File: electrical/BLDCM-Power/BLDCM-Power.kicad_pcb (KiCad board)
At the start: 4 copper layers, 32 x 32 mm, 37 parts, among them J1 501920-3001, J2 53048-0310, J3 53261-0471, J4 53261-0471, J5 FTSH-107-01-L-DV-K, J6 12402012E212A, U1 INA239-Q1, U2 LDL212PV33R, U3 TMC6300-LA, U4 INA239-Q1, U5 TCAN1462, U6 INA239-Q1

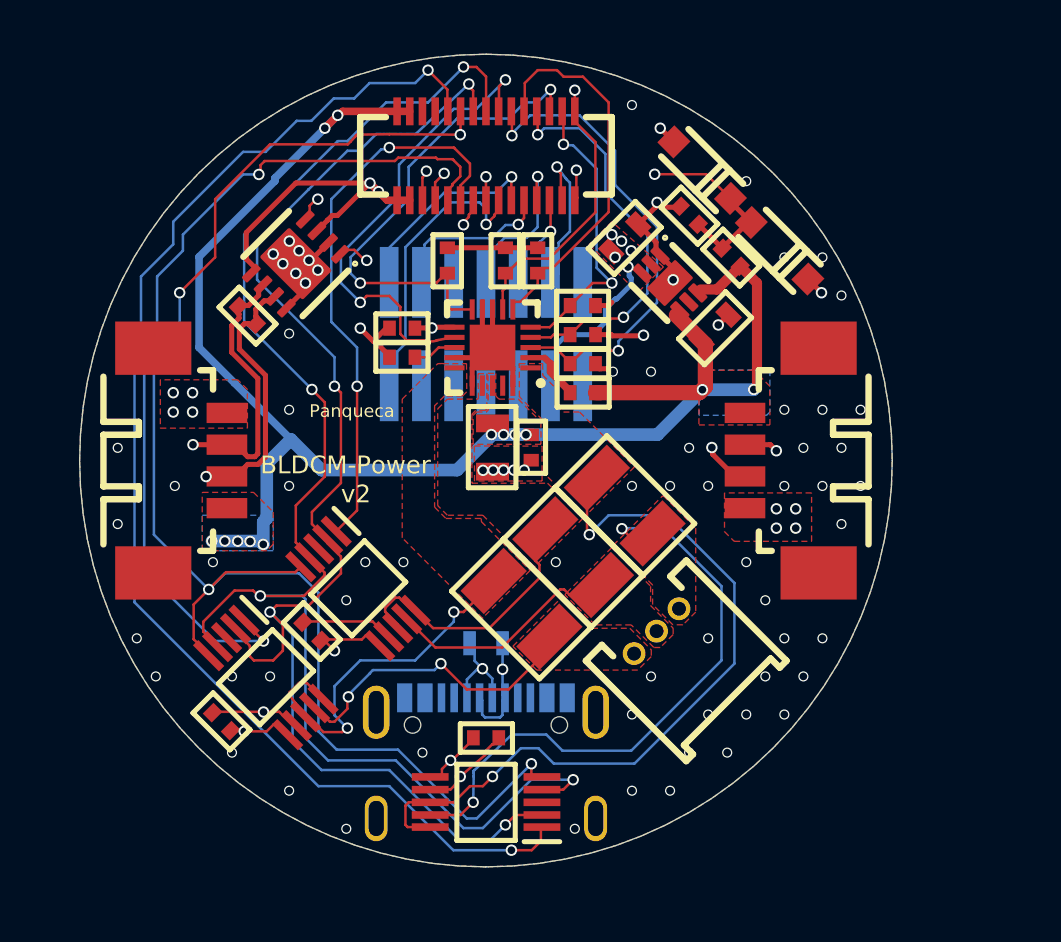
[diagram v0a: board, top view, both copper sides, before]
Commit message: Fix: PCB resistor rotation
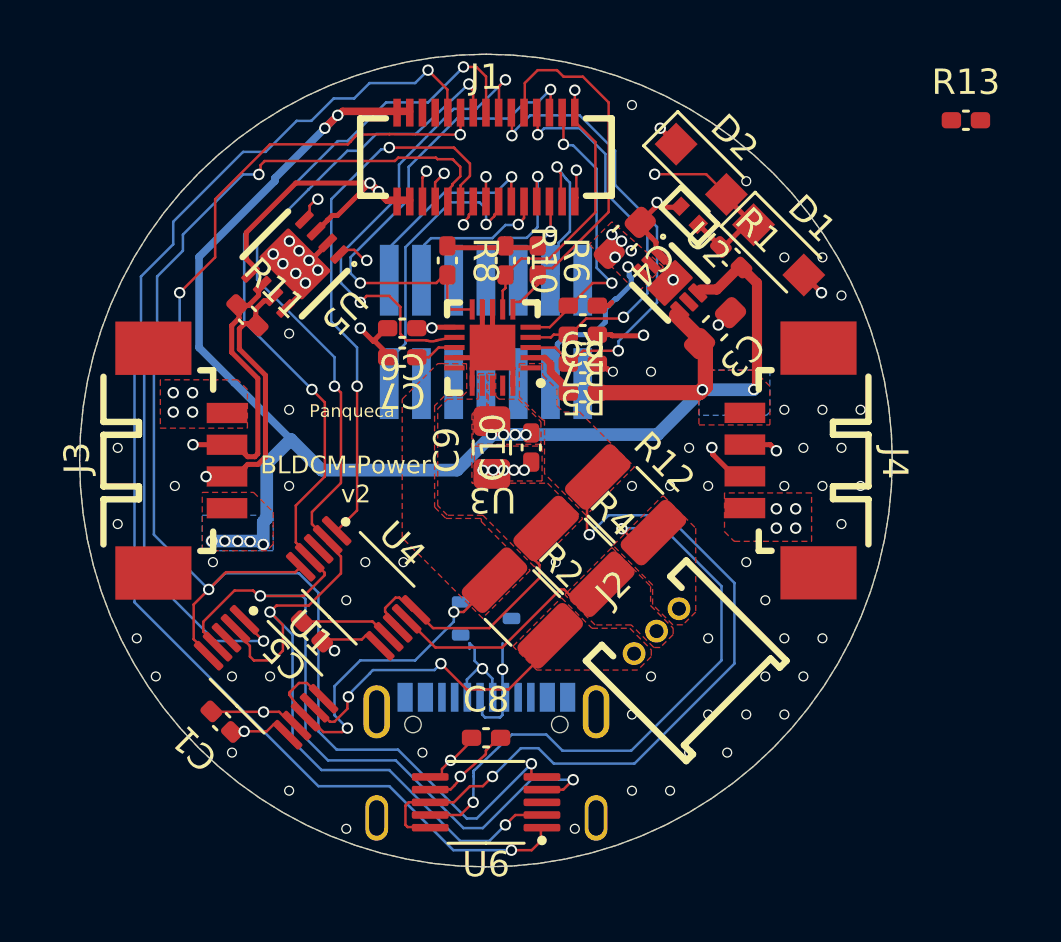
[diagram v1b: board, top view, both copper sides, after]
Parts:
- added R13: 10K, BrenoCQ:R_0402, F.Cu at (167.4, 91.6)
- C1, C10, C2, C5, C6, C7, C8: footprint brenocqLib:CAP_0402 -> BrenoCQ:C_0402
- C3, C4: footprint brenocqLib:CAP_0603 -> BrenoCQ:C_0603
- C9: footprint brenocqLib:CAP_0805 -> BrenoCQ:C_0805
- D1, D2: footprint brenocqLib:SOD-123 -> BrenoCQ:SOD-123
- D3: footprint brenocqLib:SOT-323-3 -> BrenoCQ:SOT-323
- J1: footprint brenocqLib:501920-3001 -> BrenoCQ:501920-3001
- J2: footprint brenocqLib:53048-0310 -> BrenoCQ:53048-0310
- J3, J4: footprint brenocqLib:MOLEX_125MM_4P_H_SMD -> BrenoCQ:53261-0471
- J5: footprint brenocqLib:FTSH-107-01-L-DV-K-TR -> BrenoCQ:FTSH-107-01-L-DV-K-TR
- J6: footprint brenocqLib:12402012E212A -> BrenoCQ:12402012E212A
- R1, R10, R11, R5, R6, R7, R8, R9: footprint brenocqLib:RES_0402 -> BrenoCQ:R_0402
- R12, R2, R4: footprint brenocqLib:RES_1210 -> BrenoCQ:R_1210
- U1, U4, U6: footprint brenocqLib:VSSOP-10 -> BrenoCQ:VSSOP-10
- U2: footprint brenocqLib:DFN-6-2x2 -> BrenoCQ:DFN-6-2x2
- U3: footprint brenocqLib:QFN-20 -> BrenoCQ:QFN-20
- U5: footprint brenocqLib:VSON-8 -> BrenoCQ:VSON-8
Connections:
- net CAN.RX renamed /CAN.RX
- net CAN.TX renamed /CAN.TX
- net INA.CLK renamed /INA.CLK
- net INA.CS0 renamed /INA.CS0
- net INA.CS1 renamed /INA.CS1
- net INA.CS2 renamed /INA.CS2
- net INA.PICO renamed /INA.PICO
- net INA.POCI renamed /INA.POCI
- net NetC7_1 renamed Net-(U3-1.8VOUT)
- net RST renamed /RST
- net SWCLK renamed /SWCLK
- net SWDIO renamed /SWDIO
- net SWO renamed /SWO
- net TCM.DIAG renamed /TCM.DIAG
- net TCM.U.IN renamed /TCM.U.IN
- net TCM.U.OUT renamed /TCM.U.OUT
- net TCM.V.IN renamed /TCM.V.IN
- net TCM.V.OUT renamed /TCM.V.OUT
- net TCM.W.IN renamed /TCM.W.IN
- net TCM.W.OUT renamed /TCM.W.OUT
- net USB_N renamed /USB_N
- net USB_P renamed /USB_P
- net VCP.RX renamed /VCP.RX
- net VCP.TX renamed /VCP.TX
- C1 pad 1: 3.3V -> GND
- C1 pad 2: GND -> 3.3V
- C10 pad 1: GND -> VIN
- C10 pad 2: VIN -> GND
- C2 pad 1: NetC2_1 -> VIN
- C2 pad 2: VIN -> Net-(U3-VCP)
- C3 pad 1: GND -> VIN
- C3 pad 2: VIN -> GND
- C4 pad 1: GND -> 3.3V
- C4 pad 2: 3.3V -> GND
- C5 pad 1: 3.3V -> GND
- C5 pad 2: GND -> 3.3V
- C8 pad 1: 3.3V -> GND
- C8 pad 2: GND -> 3.3V
- C9 pad 1: GND -> VIN
- C9 pad 2: VIN -> GND
- D1 pad 1: VOLT -> /VOLT
- D2 pad 2: VOLT -> /VOLT
- J1 pad 20: TMC.UH -> /TMC.UH
- J1 pad 22: TMC.UL -> /TMC.UL
- J1 pad 24: TMC.VH -> /TMC.VH
- J1 pad 26: TMC.VL -> /TMC.VL
- J1 pad 28: TMC.WH -> /TMC.WH
- J1 pad 29: VOLT -> /VOLT
- J1 pad 30: TMC.WL -> /TMC.WL
- J3 pad 2: CAN_P -> /CAN_P
- J3 pad 3: CAN_N -> /CAN_N
- J4 pad 2: CAN_P -> /CAN_P
- J4 pad 3: CAN_N -> /CAN_N
- J5 pad 1: (no net) -> unconnected-(J5-NC-Pad1)
- J5 pad 10: (no net) -> unconnected-(J5-NC-Pad10)
- J5 pad 2: (no net) -> unconnected-(J5-NC-Pad2)
- J5 pad 9: (no net) -> unconnected-(J5-NC-Pad9)
- J6 pad A4_B9: (no net) -> unconnected-(J6-VBUS-PadA4_B9)
- J6 pad A5: (no net) -> unconnected-(J6-CC1-PadA5)
- J6 pad A8: (no net) -> unconnected-(J6-SBU1-PadA8)
- J6 pad B4_A9: (no net) -> unconnected-(J6-VBUS-PadB4_A9)
- J6 pad B5: (no net) -> unconnected-(J6-CC2-PadB5)
- J6 pad B8: (no net) -> unconnected-(J6-SBU2-PadB8)
- R1 pad 1: VOLT -> VIN
- R1 pad 2: VIN -> /VOLT
- R10 pad 1: GND -> /TMC.WL
- R10 pad 2: TMC.WL -> GND
- R11 pad 1: CAN_N -> /CAN_P
- R11 pad 2: CAN_P -> /CAN_N
- R5 pad 1: GND -> /TMC.UH
- R5 pad 2: TMC.UH -> GND
- R6 pad 1: GND -> /TMC.UL
- R6 pad 2: TMC.UL -> GND
- R7 pad 1: GND -> /TMC.VH
- R7 pad 2: TMC.VH -> GND
- R8 pad 1: GND -> /TMC.VL
- R8 pad 2: TMC.VL -> GND
- R9 pad 1: GND -> /TMC.WH
- R9 pad 2: TMC.WH -> GND
- U1 pad 3: (no net) -> unconnected-(U1-ALERT-Pad3)
- U3 pad 10: TMC.VL -> /TMC.VL
- U3 pad 2: NetC2_1 -> Net-(U3-VCP)
- U3 pad 3: TMC.UH -> /TMC.UH
- U3 pad 4: TMC.VH -> /TMC.VH
- U3 pad 5: TMC.WH -> /TMC.WH
- U3 pad 6: TMC.UL -> /TMC.UL
- U3 pad 7: TMC.WL -> /TMC.WL
- U4 pad 3: (no net) -> unconnected-(U4-ALERT-Pad3)
- U5 pad 6: CAN_N -> /CAN_N
- U5 pad 7: CAN_P -> /CAN_P
- U6 pad 3: (no net) -> unconnected-(U6-ALERT-Pad3)
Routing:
- net TCM.U.IN: track 0.00 -> 14.9 mm, vias 0 -> 2
- net /TCM.U.IN: track 14.9 -> 0.00 mm, vias 2 -> 0
- net GND: track 40.1 -> 36.0 mm, vias 85 -> 80
- net /TMC.VH: track 0.00 -> 1.95 mm, vias 0 -> 1
- net /TMC.UH: track 0.00 -> 0.83 mm, vias 0 -> 1
- net /TMC.WH: track 0.00 -> 0.70 mm
- net VIN: track 63.3 -> 63.9 mm, vias 13 -> 19
- net 3.3V: vias 12 -> 9
